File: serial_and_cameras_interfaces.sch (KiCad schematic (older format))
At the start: 49 parts, among them J13 530470410, J15 530470410, J16 530470410, J17 530470410, J2 WE_68715014522, U16 NTS0102GT, U17 NTS0104PW,118, U18 MAX485EESA, U5 NTS0102GT, U6 PCA9547BS

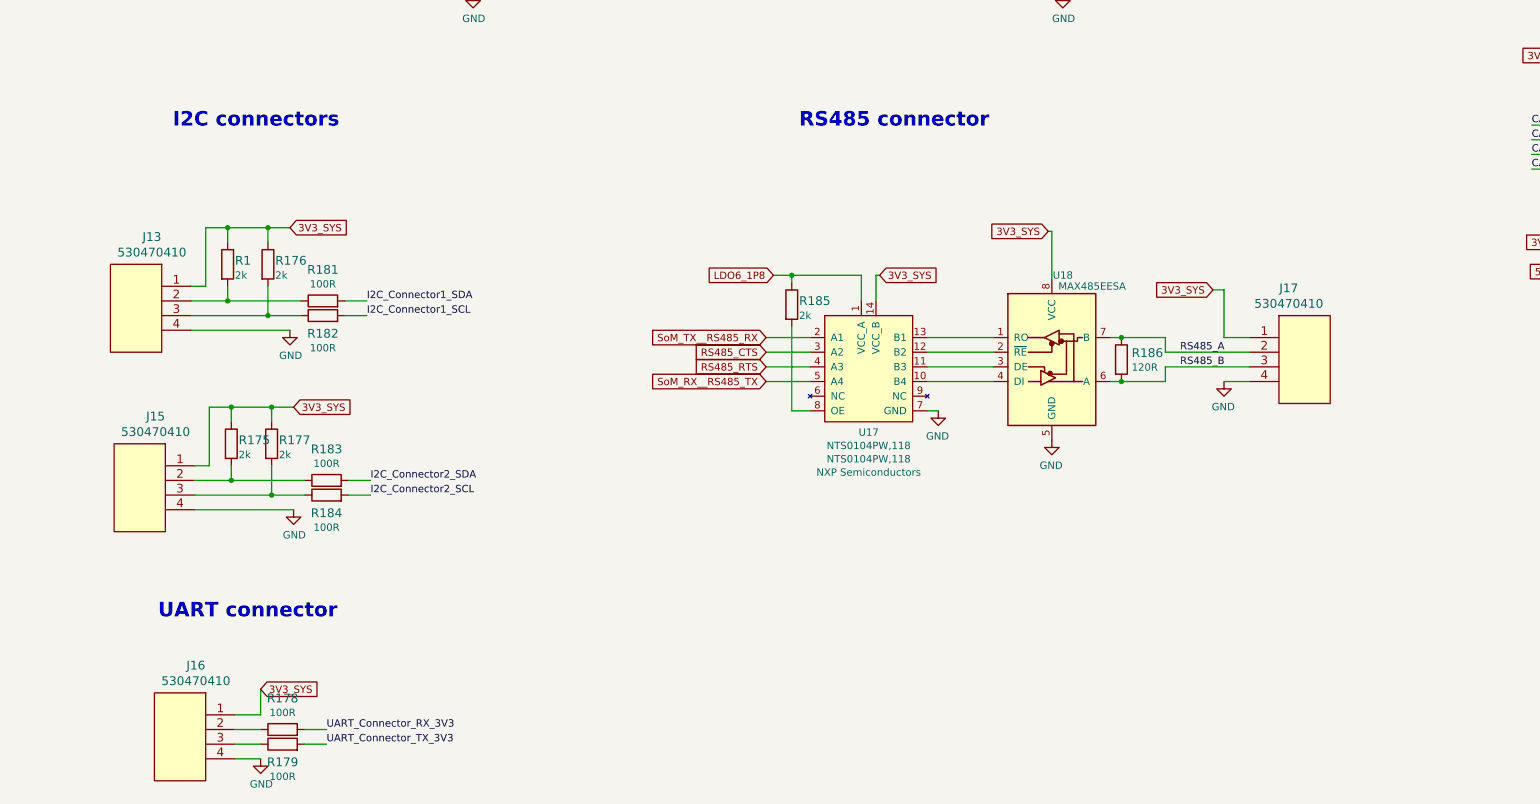
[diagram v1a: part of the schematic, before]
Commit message: Corrected serial interface schemas
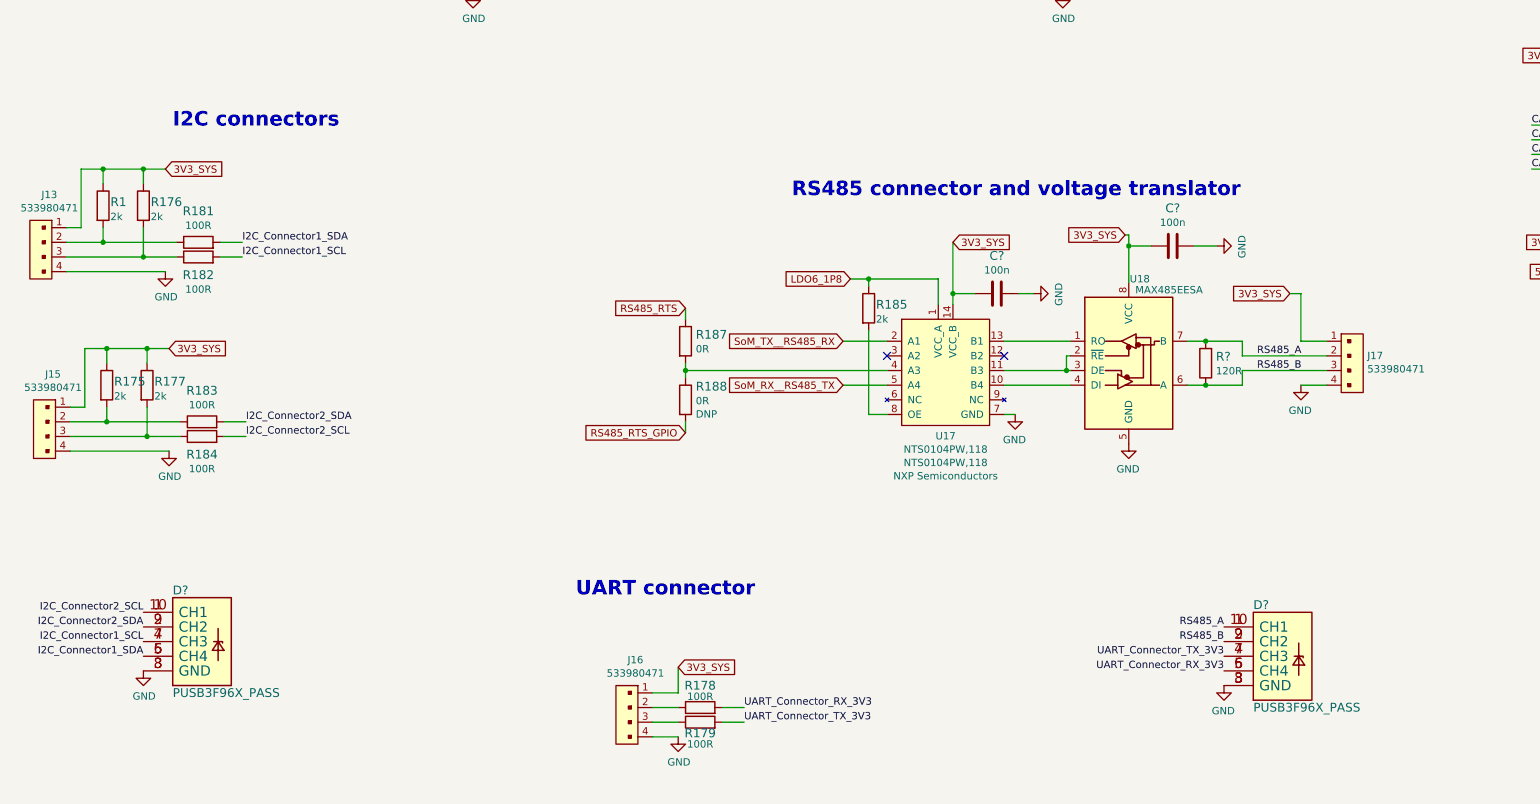
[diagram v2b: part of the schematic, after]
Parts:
- removed J13, J15, J16, J17: 530470410, sc606-baseboard-footprints:530470410, symbol sc606-baseboard:530470410
- removed R186: R_120R_0402, sc606-baseboard-footprints:0402-res, symbol sc606-baseboard:R_120R_0402
- added C? (x2): C_100n_0402, sc606-baseboard-footprints:0402-cap, symbol sc606-baseboard:C_100n_0402
- added D? (x2): PUSB3F96X_PASS, sc606-baseboard-footprints:PUSB3F96X, symbol sc606-baseboard:PUSB3F96X_PASS
- added J13, J15, J16, J17: 533980471, antmicro-footprints:Molex_PicoBlade_53398-0471_1x04-1MP_P1.25mm_Vertical, symbol antmicroRectangularConnectorsHeadersMalePins:533980471
- added R187, R188: R_0R_0402, antmicro-footprints:0402-res, symbol antmicroResistors0402:R_0R_0402
- added R?: R_120R_0603, antmicro-footprints:0603-res, symbol antmicroResistors0603:R_120R_0603
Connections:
- net 3V3_SYS: now also C?.1, C?.1, J13.1, J15.1, J16.1, J17.1
- net GND: now also C?.2, C?.2, D?.3 (GND), D?.3 (GND), D?.8 (GND), D?.8 (GND), J13.4, J15.4, J16.4, J17.4
- net I2C_Connector1_SCL: now also D?.4 (CH3), D?.7 (CH3)
- net I2C_Connector1_SDA: now also D?.5 (CH4), D?.6 (CH4)
- net I2C_Connector2_SCL: now also D?.1 (CH1), D?.10 (CH1)
- net I2C_Connector2_SDA: now also D?.2 (CH2), D?.9 (CH2)
- net RS485_A: now also D?.1 (CH1), D?.10 (CH1), J17.2, R?.2
- net RS485_B: now also D?.2 (CH2), D?.9 (CH2), J17.3, R?.1
- net RS485_RTS: now also R187.1; no longer U17.4 (A3)
- net UART_Connector_RX_3V3: now also D?.5 (CH4), D?.6 (CH4)
- net UART_Connector_TX_3V3: now also D?.4 (CH3), D?.7 (CH3)
- net at U18.2 (~RE): now also U17.11 (B3), U18.3 (DE); no longer U17.12 (B2)
- net at R1.2, R181.1: now also J13.2
- net at R176.2, R182.1: now also J13.3
- net at R175.2, R183.1: now also J15.2
- net at R177.2, R184.1: now also J15.3
- net at R178.1: now also J16.2
- net at R179.1: now also J16.3
- net RS485_CTS: no longer names the net of U17.3 (A2)
- new net: R187.2, R188.1, U17.4 (A3)
- new net RS485_RTS_GPIO: R188.2
- no-connect marks 18 -> 20
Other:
- note added: "RS485 connector and voltage translator\n"
- note removed: "RS485 connector\n"
- moved on the sheet: R1, R175, R176, R177, R178, R179, R181, R182, R183, R184, R185, U17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

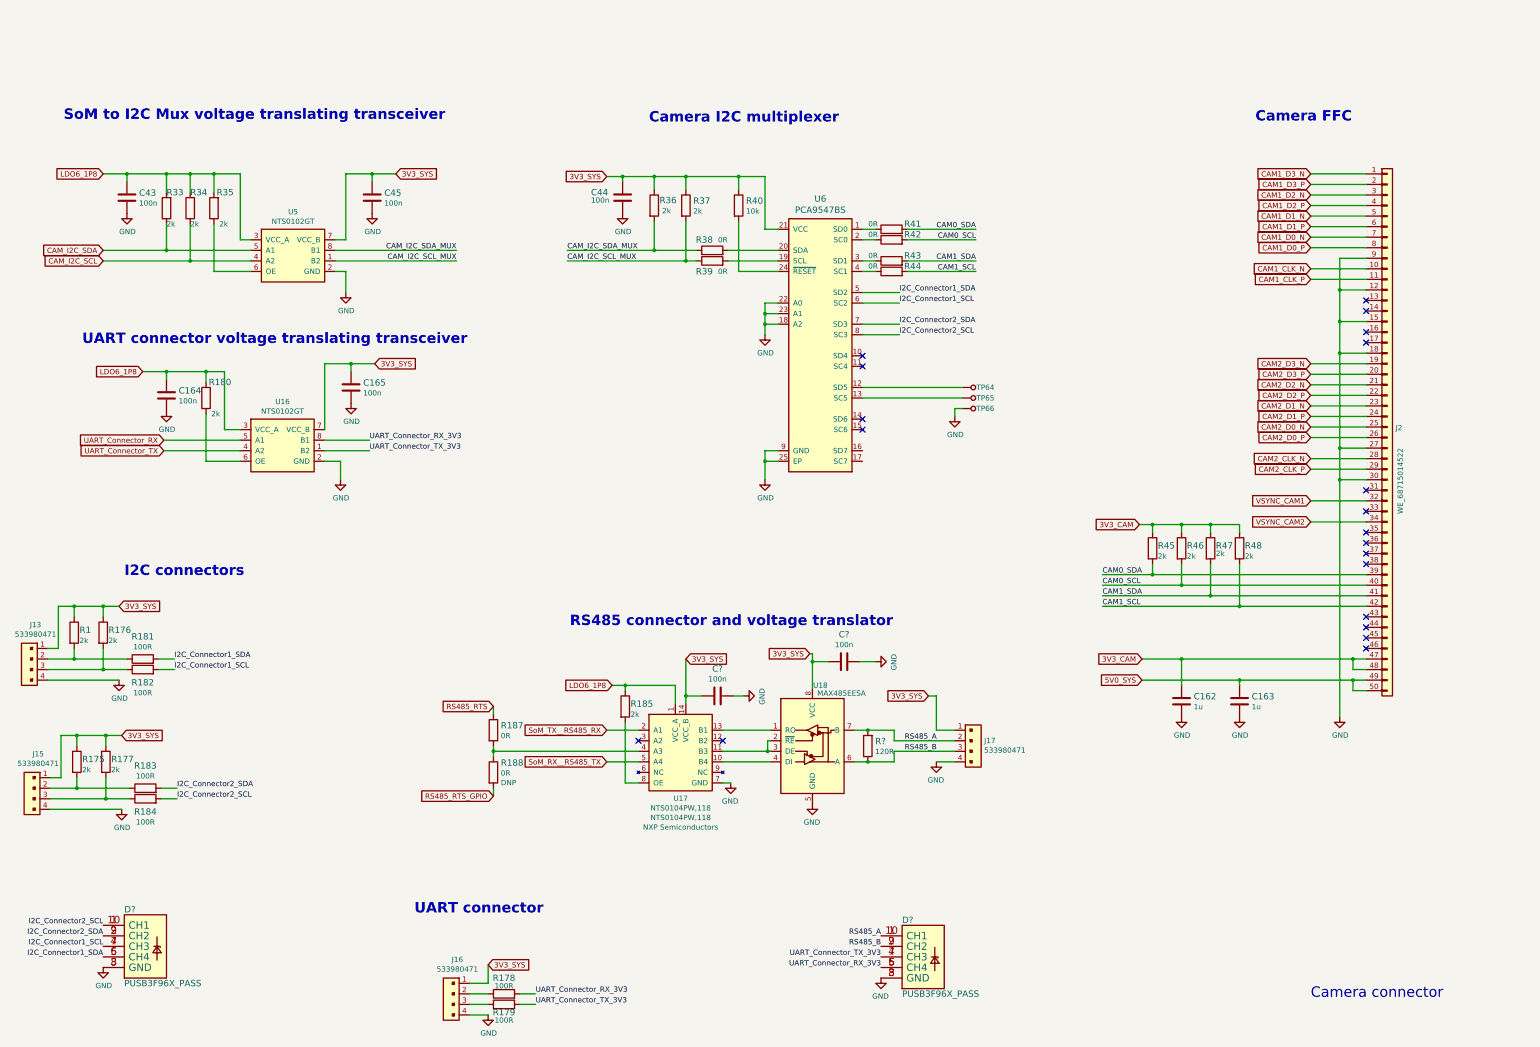
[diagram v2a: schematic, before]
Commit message: Cleaned serial interfaces
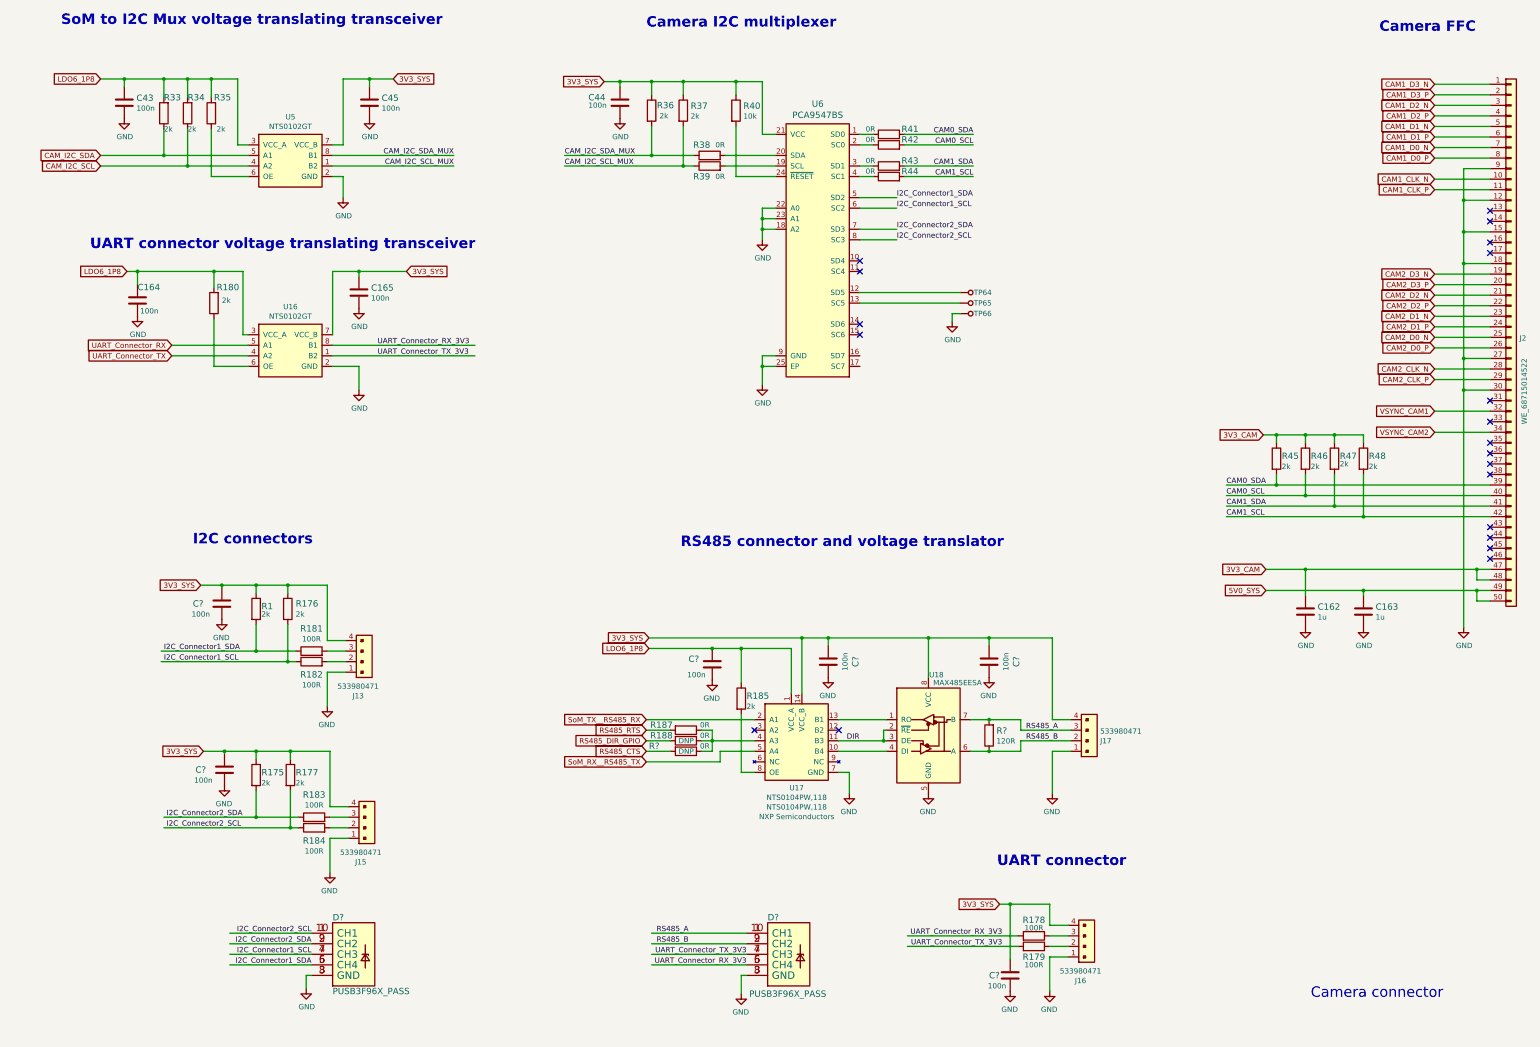
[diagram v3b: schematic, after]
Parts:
- removed C?: C_100n_0402, sc606-baseboard-footprints:0402-cap, symbol sc606-baseboard:C_100n_0402
- added C? (x5): C_100n_0402, sc606-baseboard-footprints:0402-cap, symbol sc606-baseboard:C_100n_0402
- added R?: R_0R_0402, antmicro-footprints:0402-res, symbol antmicroResistors0402:R_0R_0402
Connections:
- net labels added: DIR, RS485_CTS, RS485_DIR_GPIO
- net labels removed: RS485_RTS_GPIO
- wire segments 240 -> 270
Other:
- moved on the sheet: C162, C163, C164, C165, C43, C44, C45, C?, D?, J13, J15, J16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
